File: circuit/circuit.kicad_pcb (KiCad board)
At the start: 4 copper layers, 175.5 x 119.5 mm, 206 parts, among them J201 Barrel_Jack, J301 FX_R_2, J302 FX_R_4, J303 FX_R_6, J304 FX_R_8, J305 FX_R_1, J306 FX_R_3, J307 FX_R_5, J308 FX_R_7, J309 FX_S_1, J310 FX_S_2, J311 FX_S_3, J312 FX_S_4, J313 FX_S_5, J314 FX_S_6, J315 FX_S_7, J316 FX_S_8, J317 Guitar_In, J318 Amp_Out, SW101 Pedal_1, SW102 Pedal_2, SW103 Pedal_3, SW104 Pedal_4, SW105 Pedal_5, SW106 Pedal_6, SW107 Pedal_7, SW108 Pedal_8, SW109 Program, SW110 Preset, U101 ESP32-S3-DevKitC, U201 TMA-1215D, U202 LM7805_TO220, U203 LM7905_TO220, U204 LM1117T-3.3, U301 TL072, U302 TL072, U303 TL072, U304 TL072, U305 TL072, U306 TL072, U307 TL072, U308 TL072, U309 TL072, U401 ADG419BN, U402 CD4051B, U501 CD4051B, U502 CD4051B, U503 CD4051B, U504 CD4051B, U601 CD4051B, U602 CD4051B, U603 CD4051B, U604 CD4051B, U701 74HC595, U702 74HC595, U703 74HC595, U704 74HC595, U801 74HC595, U802 74HC595, U901 74HC595, U902 74HC595

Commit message: Circuit tweaks and PCB
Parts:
- removed L309, L310: 600R@100Mhz, WE-UKW:WE-UKW_74275010
- added C337: 1uF, Capacitor_THT:C_Disc_D3.0mm_W2.0mm_P2.50mm, F.Cu at (122.0, 84.0)
- added L303: 600R@100Mhz, WE-UKW:WE-UKW_74275010, F.Cu at (87.5, 65.5)
- added L304: 600R@100Mhz, WE-UKW:WE-UKW_74275010, F.Cu at (89.0, 79.0)
- C309, C310, C311, C312, C313, C314, C315, C316, C317, C318: value 0.1uF -> 1uF
- C325, C326, C327, C328, C329, C330, C331, C332, C333, C336: value 1uF -> 0.1uF
- D201: value 1N4007 -> 1N5822
- J301: value FX_R_2 -> FX_R_1
- J302: value FX_R_4 -> FX_R_2
- J303: value FX_R_6 -> FX_R_3
- J304: value FX_R_8 -> FX_R_4
- J305: value FX_R_1 -> FX_R_5
- J306: value FX_R_3 -> FX_R_6
- J307: value FX_R_5 -> FX_R_7
- J308: value FX_R_7 -> FX_R_8
- SW102: value Pedal_2 -> Pedal_6
- SW103: value Pedal_3 -> Pedal_2
- SW104: value Pedal_4 -> Pedal_7
- SW105: value Pedal_5 -> Pedal_3
- SW106: value Pedal_6 -> Pedal_8
- SW107: value Pedal_7 -> Pedal_4
- SW108: value Pedal_8 -> Program
- SW109: value Program -> Pedal_5
- moved R902 79.6 mm to (156.7, 133.5)
- moved C318 78.7 mm to (153.5, 46.5), turned to -90 degrees
- moved C314 77.4 mm to (127.4, 46.5), turned to -90 degrees
- moved C110 76.5 mm to (211.5, 39.0)
- moved SW110 76.5 mm to (209.0, 44.0)
- moved C316 75.3 mm to (140.4, 46.5), turned to -90 degrees
- moved R901 73.2 mm to (156.7, 129.0)
- moved R907 72.0 mm to (178.9, 133.5)
- moved C310 70.6 mm to (101.2, 46.5), turned to -90 degrees
- moved R908 69.6 mm to (190.0, 128.9)
- moved C312 68.7 mm to (114.3, 46.5), turned to -90 degrees
- moved R904 68.4 mm to (167.8, 133.4)
- moved C317 66.7 mm to (147.0, 46.5), turned to -90 degrees
- moved C313 66.3 mm to (120.8, 46.5), turned to -90 degrees
- moved R905 65.8 mm to (178.9, 129.0)
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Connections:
- C102 pad 2: Net-(U101-GPIO7/ADC1_CH6) -> Net-(U101-GPIO11/ADC2_CH0)
- C103 pad 2: Net-(U101-GPIO8/ADC1_CH7) -> Net-(U101-GPIO7/ADC1_CH6)
- C104 pad 2: Net-(U101-GPIO9/ADC1_CH8) -> Net-(U101-GPIO12/ADC2_CH1)
- C105 pad 2: Net-(U101-GPIO10/ADC1_CH9) -> Net-(U101-GPIO8/ADC1_CH7)
- C106 pad 2: Net-(U101-GPIO11/ADC2_CH0) -> Net-(U101-GPIO13/ADC2_CH2)
- C107 pad 2: Net-(U101-GPIO12/ADC2_CH1) -> Net-(U101-GPIO9/ADC1_CH8)
- C108 pad 2: Net-(U101-GPIO13/ADC2_CH2) -> Net-(U101-GPIO14/ADC2_CH3)
- C109 pad 2: Net-(U101-GPIO14/ADC2_CH3) -> Net-(U101-GPIO10/ADC1_CH9)
- C309 pad 1: _15V_F -> Net-(C309-Pad1)
- C309 pad 2: AGND -> Net-(C309-Pad2)
- C310 pad 1: _15V_F -> Net-(C310-Pad1)
- C310 pad 2: AGND -> Net-(C310-Pad2)
- C311 pad 1: _15V_F -> Net-(C311-Pad1)
- C311 pad 2: AGND -> Net-(C311-Pad2)
- C312 pad 1: _15V_F -> Net-(C312-Pad1)
- C312 pad 2: AGND -> Net-(C312-Pad2)
- C313 pad 1: AGND -> Net-(C313-Pad1)
- C313 pad 2: +15V_F -> Net-(C313-Pad2)
- C314 pad 1: AGND -> Net-(C314-Pad1)
- C314 pad 2: +15V_F -> Net-(C314-Pad2)
- C315 pad 1: AGND -> Net-(C315-Pad1)
- C315 pad 2: +15V_F -> Net-(C315-Pad2)
- C316 pad 1: AGND -> Net-(C316-Pad1)
- C316 pad 2: +15V_F -> Net-(C316-Pad2)
- C317 pad 1: Net-(U305-V-) -> Net-(C317-Pad1)
- C317 pad 2: AGND -> Net-(C317-Pad2)
- C318 pad 1: Net-(U305-V-) -> Net-(C318-Pad1)
- C318 pad 2: AGND -> Net-(U309-2-)
- C319 pad 1: Net-(U305-V-) -> AGND
- C319 pad 2: AGND -> +15V_F
- C320 pad 1: Net-(U305-V-) -> -15V_F
- C321 pad 2: Net-(U305-V+) -> +15V_F
- C322 pad 1: AGND -> -15V_F
- C322 pad 2: Net-(U305-V+) -> AGND
- C323 pad 2: Net-(U305-V+) -> +15V_F
- C324 pad 1: AGND -> -15V_F
- C324 pad 2: Net-(U305-V+) -> AGND
- C325 pad 1: Net-(C325-Pad1) -> AGND
- C325 pad 2: Net-(C325-Pad2) -> +15V_F
- C326 pad 1: Net-(C326-Pad1) -> -15V_F
- C326 pad 2: Net-(C326-Pad2) -> AGND
- C327 pad 1: Net-(C327-Pad1) -> AGND
- C327 pad 2: Net-(C327-Pad2) -> Net-(U305-V+)
- C328 pad 1: Net-(C328-Pad1) -> Net-(U305-V-)
- C328 pad 2: Net-(C328-Pad2) -> AGND
- C329 pad 1: Net-(C329-Pad1) -> AGND
- C329 pad 2: Net-(C329-Pad2) -> Net-(U305-V+)
- C330 pad 1: Net-(C330-Pad1) -> Net-(U305-V-)
- C330 pad 2: Net-(C330-Pad2) -> AGND
- C331 pad 1: Net-(C331-Pad1) -> AGND
- C331 pad 2: Net-(C331-Pad2) -> Net-(U305-V+)
- C332 pad 1: Net-(C332-Pad1) -> Net-(U305-V-)
- C332 pad 2: Net-(C332-Pad2) -> AGND
- C333 pad 1: Net-(C333-Pad1) -> AGND
- C333 pad 2: Net-(C333-Pad2) -> Net-(U305-V+)
- C336 pad 1: Net-(U309-1-) -> Net-(U305-V-)
- C336 pad 2: GUITAR_IN -> AGND
- C402 pad 1: +5V_F -> -15V_F
- C403 pad 1: -5V_F -> +5V_F
- C404 pad 1: AGND -> -5V_F
- C404 pad 2: +5V_F -> AGND
- C405 pad 1: -15V_F -> AGND
- C405 pad 2: AGND -> +5V_F
- C501 pad 1: AGND -> -5V_F
- C501 pad 2: +5V_F -> AGND
- C503 pad 1: AGND -> -5V_F
- C503 pad 2: +5V_F -> AGND
- C504 pad 1: -5V_F -> AGND
- C504 pad 2: AGND -> +5V_F
- C506 pad 1: -5V_F -> AGND
- C506 pad 2: AGND -> +5V_F
- C507 pad 1: AGND -> -5V_F
- C507 pad 2: +5V_F -> AGND
- C508 pad 1: -5V_F -> AGND
- C508 pad 2: AGND -> +5V_F
- C601 pad 1: AGND -> Net-(U601-VEE)
- C601 pad 2: Net-(U601-VDD) -> AGND
- C602 pad 1: AGND -> Net-(U601-VEE)
- C602 pad 2: Net-(U601-VDD) -> AGND
- C604 pad 1: Net-(U601-VEE) -> AGND
- C604 pad 2: AGND -> Net-(U601-VDD)
- C606 pad 1: Net-(U601-VEE) -> AGND
- C606 pad 2: AGND -> Net-(U601-VDD)
- C607 pad 1: AGND -> Net-(U601-VEE)
- C607 pad 2: Net-(U601-VDD) -> AGND
- C608 pad 1: Net-(U601-VEE) -> AGND
- C608 pad 2: AGND -> Net-(U601-VDD)
- J201 pad 1: GND -> /Power/12V_RAW_1
- J201 pad 2: /Power/12V_RAW_1 -> GND
- J301 pad T: Net-(C303-Pad1) -> Net-(C301-Pad1)
- J302 pad T: Net-(C304-Pad1) -> Net-(C302-Pad1)
- J303 pad T: Net-(C301-Pad1) -> Net-(C303-Pad1)
- J304 pad T: Net-(C302-Pad1) -> Net-(C304-Pad1)
- J309 pad T: Net-(C325-Pad1) -> Net-(C309-Pad1)
- J310 pad T: Net-(C326-Pad1) -> Net-(C310-Pad1)
- J311 pad T: Net-(C327-Pad1) -> Net-(C311-Pad1)
- J312 pad T: Net-(C328-Pad1) -> Net-(C312-Pad1)
- J313 pad T: Net-(C329-Pad1) -> Net-(C313-Pad1)
- J314 pad T: Net-(C330-Pad1) -> Net-(C314-Pad1)
- J315 pad T: Net-(C331-Pad1) -> Net-(C315-Pad1)
- J316 pad T: Net-(C332-Pad1) -> Net-(C316-Pad1)
- J317 pad T: Net-(C333-Pad1) -> Net-(C317-Pad1)
- J318 pad T: Net-(U309-2-) -> Net-(C318-Pad1)
- L301 pad 1: +15V -> +15V_F
- L301 pad 2: +15V_F -> +15V
- L302 pad 1: _15V_F -> -15V
- L302 pad 2: -15V -> -15V_F
- R301 pad 1: Net-(U301-2+) -> Net-(U301-1+)
- R301 pad 2: Net-(C303-Pad2) -> Net-(C301-Pad2)
- R302 pad 1: Net-(U304-2+) -> Net-(U301-2+)
- R303 pad 1: Net-(U302-2+) -> Net-(U302-1+)
- R303 pad 2: Net-(C304-Pad2) -> Net-(C303-Pad2)
- R304 pad 1: Net-(U303-2+) -> Net-(U302-2+)
- R304 pad 2: Net-(C301-Pad2) -> Net-(C304-Pad2)
- R305 pad 1: Net-(U301-1+) -> Net-(U303-1+)
- R306 pad 1: Net-(U302-1+) -> Net-(U303-2+)
- R307 pad 1: Net-(U303-1+) -> Net-(U304-1+)
- R308 pad 1: Net-(U304-1+) -> Net-(U304-2+)
- R309 pad 2: Net-(C325-Pad2) -> Net-(C309-Pad2)
- R310 pad 2: Net-(C326-Pad2) -> Net-(C310-Pad2)
- R311 pad 2: Net-(C327-Pad2) -> Net-(C311-Pad2)
- R312 pad 2: Net-(C328-Pad2) -> Net-(C312-Pad2)
- R313 pad 2: Net-(C329-Pad2) -> Net-(C313-Pad2)
- R314 pad 2: Net-(C330-Pad2) -> Net-(C314-Pad2)
- R315 pad 2: Net-(C331-Pad2) -> Net-(C315-Pad2)
- R316 pad 2: Net-(C332-Pad2) -> Net-(C316-Pad2)
- R317 pad 2: Net-(C333-Pad2) -> Net-(C317-Pad2)
- SW102 pad 1: Net-(U101-GPIO7/ADC1_CH6) -> Net-(U101-GPIO11/ADC2_CH0)
- SW103 pad 1: Net-(U101-GPIO8/ADC1_CH7) -> Net-(U101-GPIO7/ADC1_CH6)
- SW104 pad 1: Net-(U101-GPIO9/ADC1_CH8) -> Net-(U101-GPIO12/ADC2_CH1)
- SW105 pad 1: Net-(U101-GPIO10/ADC1_CH9) -> Net-(U101-GPIO8/ADC1_CH7)
- SW106 pad 1: Net-(U101-GPIO11/ADC2_CH0) -> Net-(U101-GPIO13/ADC2_CH2)
- SW107 pad 1: Net-(U101-GPIO12/ADC2_CH1) -> Net-(U101-GPIO9/ADC1_CH8)
- SW108 pad 1: Net-(U101-GPIO13/ADC2_CH2) -> Net-(U101-GPIO14/ADC2_CH3)
- SW109 pad 1: Net-(U101-GPIO14/ADC2_CH3) -> Net-(U101-GPIO10/ADC1_CH9)
- U301 pad 4: _15V_F -> -15V_F
- U302 pad 4: _15V_F -> -15V_F
- U303 pad 4: _15V_F -> -15V_F
- U304 pad 4: _15V_F -> -15V_F
- U501 pad 10: /Matrix Shift Registers/U8_Q3 -> /IO Routing/U7_Q5
- U501 pad 11: /Matrix Shift Registers/U8_Q2 -> /IO Routing/U7_Q4
- U501 pad 14: FX_R_1 -> FX_R_2
- U501 pad 15: FX_R_2 -> FX_R_3
- U501 pad 3: FX_S_3 -> FX_S_1
- U501 pad 6: /IO Routing/U901_Q3 -> /IO Routing/U901_Q1
- U501 pad 9: /Matrix Shift Registers/U8_Q4 -> /IO Routing/U7_Q6
- U502 pad 10: /IO Routing/U7_Q5 -> /Matrix Shift Registers/U8_Q6
- U502 pad 11: /IO Routing/U7_Q4 -> /Matrix Shift Registers/U8_Q5
- U502 pad 12: FX_R_4 -> FX_R_3
- U502 pad 14: FX_R_2 -> FX_R_1
- U502 pad 15: FX_R_3 -> FX_R_2
- U502 pad 3: FX_S_1 -> FX_S_4
- U502 pad 6: /IO Routing/U901_Q1 -> /IO Routing/U901_Q4
- U502 pad 9: /IO Routing/U7_Q6 -> /Matrix Shift Registers/U8_Q7
- U504 pad 10: /Matrix Shift Registers/U8_Q6 -> /Matrix Shift Registers/U8_Q3
- U504 pad 11: /Matrix Shift Registers/U8_Q5 -> /Matrix Shift Registers/U8_Q2
- U504 pad 12: FX_R_3 -> FX_R_4
- U504 pad 3: FX_S_4 -> FX_S_3
- U504 pad 6: /IO Routing/U901_Q4 -> /IO Routing/U901_Q3
- U504 pad 9: /Matrix Shift Registers/U8_Q7 -> /Matrix Shift Registers/U8_Q4
- U602 pad 10: /Matrix Shift Registers/U9_Q4 -> /Matrix Shift Registers/U10_Q2
- U602 pad 11: /Matrix Shift Registers/U9_Q3 -> /Matrix Shift Registers/U10_Q1
- U602 pad 2: FX_R_7 -> FX_R_6
- U602 pad 3: FX_S_6 -> FX_S_8
- U602 pad 4: FX_R_8 -> FX_R_7
- U602 pad 6: /Inhibit Registers/U902_Q1 -> /Inhibit Registers/U902_Q3
- U602 pad 9: /Matrix Shift Registers/U9_Q5 -> /Matrix Shift Registers/U10_Q3
- U603 pad 10: /Matrix Shift Registers/U9_Q7 -> /Matrix Shift Registers/U9_Q4
- U603 pad 11: /Matrix Shift Registers/U9_Q6 -> /Matrix Shift Registers/U9_Q3
- U603 pad 2: FX_R_6 -> FX_R_7
- U603 pad 3: FX_S_7 -> FX_S_6
- U603 pad 6: /Inhibit Registers/U902_Q2 -> /Inhibit Registers/U902_Q1
- U603 pad 9: /Matrix Shift Registers/U10_Q0 -> /Matrix Shift Registers/U9_Q5
- U604 pad 10: /Matrix Shift Registers/U10_Q2 -> /Matrix Shift Registers/U9_Q7
- U604 pad 11: /Matrix Shift Registers/U10_Q1 -> /Matrix Shift Registers/U9_Q6
- U604 pad 3: FX_S_8 -> FX_S_7
- U604 pad 4: FX_R_7 -> FX_R_8
- U604 pad 6: /Inhibit Registers/U902_Q3 -> /Inhibit Registers/U902_Q2
- U604 pad 9: /Matrix Shift Registers/U10_Q3 -> /Matrix Shift Registers/U10_Q0
- U702 pad 1: /Matrix Shift Registers/U8_Q1 -> /Matrix Shift Registers/U9_Q1
- U702 pad 14: Net-(U701-QH') -> Net-(U702-SER)
- U702 pad 15: /Matrix Shift Registers/U8_Q0 -> /Matrix Shift Registers/U9_Q0
- U702 pad 2: /Matrix Shift Registers/U8_Q2 -> /Matrix Shift Registers/U9_Q2
- U702 pad 3: /Matrix Shift Registers/U8_Q3 -> /Matrix Shift Registers/U9_Q3
- U702 pad 4: /Matrix Shift Registers/U8_Q4 -> /Matrix Shift Registers/U9_Q4
- U702 pad 5: /Matrix Shift Registers/U8_Q5 -> /Matrix Shift Registers/U9_Q5
- U702 pad 6: /Matrix Shift Registers/U8_Q6 -> /Matrix Shift Registers/U9_Q6
- U702 pad 7: /Matrix Shift Registers/U8_Q7 -> /Matrix Shift Registers/U9_Q7
- U703 pad 1: /Matrix Shift Registers/U9_Q1 -> /Matrix Shift Registers/U8_Q1
- U703 pad 14: Net-(U702-QH') -> Net-(U701-QH')
- U703 pad 15: /Matrix Shift Registers/U9_Q0 -> /Matrix Shift Registers/U8_Q0
- U703 pad 2: /Matrix Shift Registers/U9_Q2 -> /Matrix Shift Registers/U8_Q2
- U703 pad 3: /Matrix Shift Registers/U9_Q3 -> /Matrix Shift Registers/U8_Q3
- U703 pad 4: /Matrix Shift Registers/U9_Q4 -> /Matrix Shift Registers/U8_Q4
- U703 pad 5: /Matrix Shift Registers/U9_Q5 -> /Matrix Shift Registers/U8_Q5
- U703 pad 6: /Matrix Shift Registers/U9_Q6 -> /Matrix Shift Registers/U8_Q6
- U703 pad 7: /Matrix Shift Registers/U9_Q7 -> /Matrix Shift Registers/U8_Q7
- U703 pad 9: Net-(U703-QH') -> Net-(U702-SER)
- U704 pad 14: Net-(U703-QH') -> Net-(U702-QH')
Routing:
- net /Matrix Shift Registers/U8_Q0: track 22.9 -> 162.7 mm
- net /Inhibit Registers/U902_Q0: track 70.7 -> 202.7 mm
- net FX_S_1: track 147.4 -> 31.7 mm
- net /Matrix Shift Registers/U8_Q3: track 40.5 -> 150.4 mm
- net /IO Routing/U7_Q4: track 75.8 -> 185.8 mm
- net /IO Routing/U901_Q1: track 187.3 -> 82.1 mm
- net Net-(Disp101-SDA): track 69.6 -> 168.5 mm
- net /Matrix Shift Registers/U8_Q4: track 43.1 -> 139.8 mm
- net Net-(U101-GPIO14/ADC2_CH3): track 77.2 -> 169.9 mm
- net -15V_F: track 9.39 -> 78.6 mm
- net /Matrix Shift Registers/U8_Q2: track 43.1 -> 109.3 mm
- net /Matrix Shift Registers/U8_Q1: track 22.4 -> 87.6 mm
- net _15V_F: track 62.3 -> 0.00 mm
- net Net-(U101-GPIO15/ADC2_CH4/32K_P): track 147.5 -> 86.1 mm
- net Net-(U601-VDD): track 66.2 -> 127.1 mm
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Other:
- board size 175.5 x 119.5 mm -> 175.5 x 120.8 mm

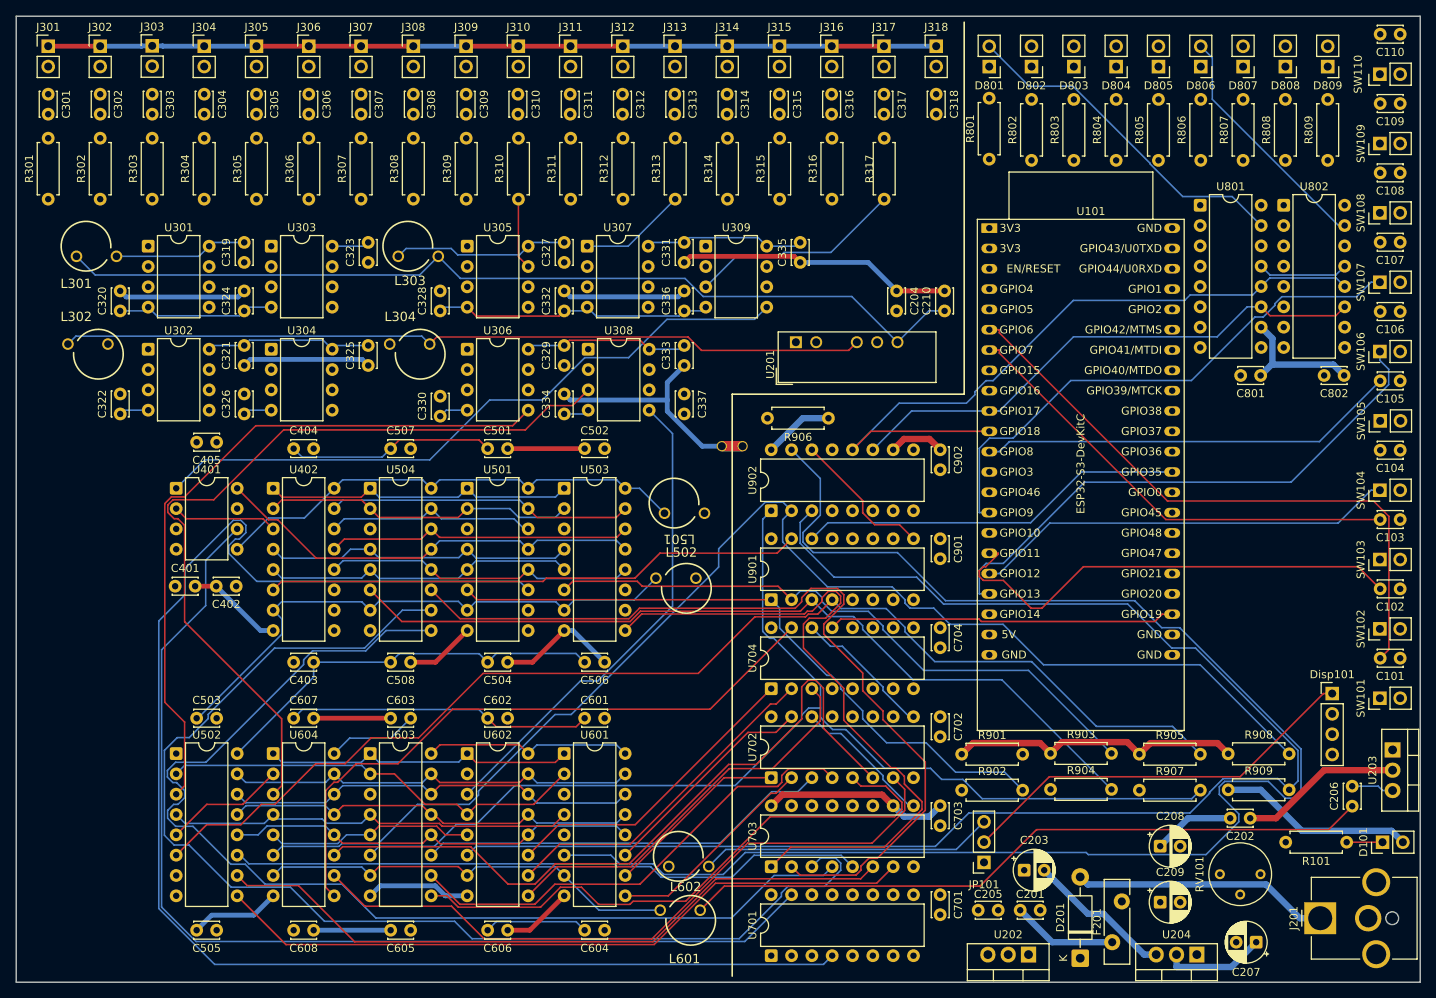
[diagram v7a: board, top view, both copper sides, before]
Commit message: Labels for headers on PCB
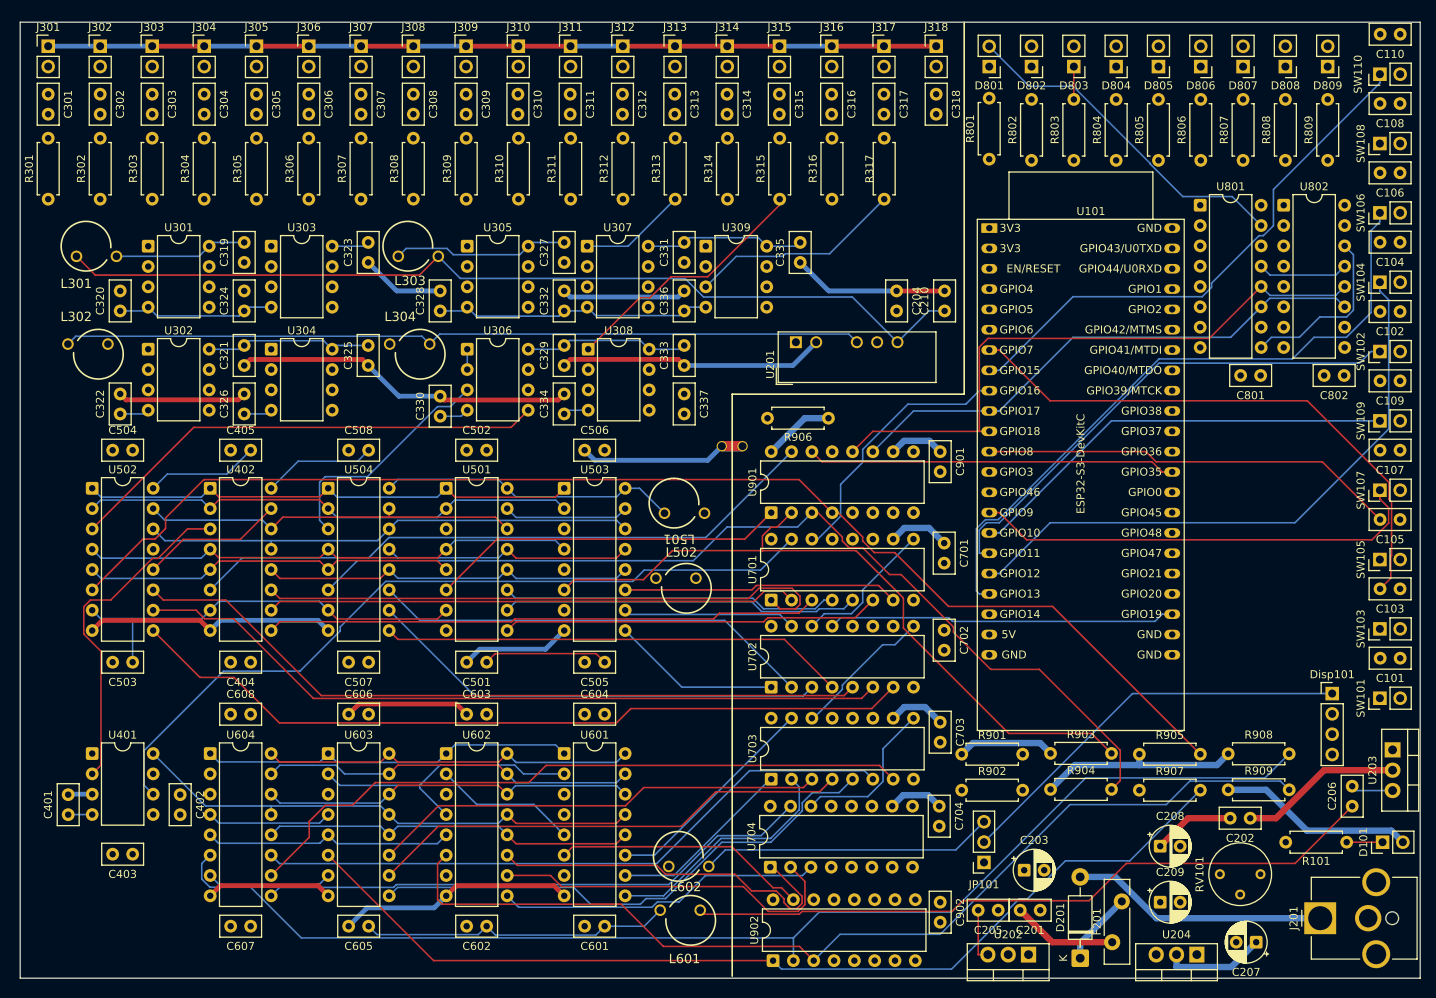
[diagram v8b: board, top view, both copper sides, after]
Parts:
- C101, C102, C103, C104, C105, C106, C107, C108, C109, C110, C201, C202, C204, C205, C206, C210, C301, C302, C303, C304, C305, C306, C307, C308, C309, C310, C311, C312, C313, C314, C315, C316, C317, C318, C319, C320, C321, C322, C323, C324, C325, C326, C327, C328, C329, C330, C331, C332, C333, C334, C335, C336, C337, C401, C402, C403, C404, C405, C501, C502, C503, C504, C505, C506, C507, C508, C601, C602, C603, C604, C605, C606, C607, C608, C701, C702, C703, C704, C801, C802, C901, C902: footprint Capacitor_THT:C_Disc_D3.0mm_W2.0mm_P2.50mm -> Capacitor_THT:C_Disc_D5.0mm_W2.5mm_P2.50mm
- moved C505 58.9 mm to (112.1, 117.5)
- moved C902 56.6 mm to (154.0, 147.5)
- moved U902 56.2 mm to (133.1, 154.8)
- moved C504 56.0 mm to (50.6, 91.0), turned to 0 degrees
- moved U701 44.4 mm to (132.9, 109.7)
- moved C701 44.0 mm to (154.5, 102.6)
- moved U401 34.8 mm to (48.0, 128.9)
- moved U502 34.8 mm to (48.0, 95.8)
- moved C109 34.7 mm to (211.5, 82.3)
- moved C102 34.7 mm to (211.5, 73.7)
- moved SW109 34.7 mm to (209.0, 87.3)
- moved SW102 34.7 mm to (209.0, 78.7)
- moved C606 33.5 mm to (80.1, 124.0), turned to 0 degrees
- moved C403 33.0 mm to (53.1, 141.5)
- moved C401 31.5 mm to (45.0, 136.6), turned to 90 degrees
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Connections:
- net /IO Routing/U7_Q0 renamed /IO Routing/U701_Q0
- net /IO Routing/U7_Q1 renamed /IO Routing/U701_Q1
- net /IO Routing/U7_Q2 renamed /IO Routing/U701_Q2
- net /IO Routing/U7_Q3 renamed /IO Routing/U701_Q3
- net /IO Routing/U7_Q4 renamed /IO Routing/U701_Q4
- net /IO Routing/U7_Q5 renamed /IO Routing/U701_Q5
- net /IO Routing/U7_Q6 renamed /IO Routing/U701_Q6
- net /IO Routing/U7_Q7 renamed /IO Routing/U701_Q7
- net /Matrix Shift Registers/U10_Q0 renamed /Matrix Shift Registers/U704_Q0
- net /Matrix Shift Registers/U10_Q1 renamed /Matrix Shift Registers/U704_Q1
- net /Matrix Shift Registers/U10_Q2 renamed /Matrix Shift Registers/U704_Q2
- net /Matrix Shift Registers/U10_Q3 renamed /Matrix Shift Registers/U704_Q3
- U502 pad 10: /Matrix Shift Registers/U8_Q6 -> /Matrix Shift Registers/U702_Q6
- U502 pad 11: /Matrix Shift Registers/U8_Q5 -> /Matrix Shift Registers/U702_Q5
- U502 pad 9: /Matrix Shift Registers/U8_Q7 -> /Matrix Shift Registers/U702_Q7
- U503 pad 10: /Matrix Shift Registers/U8_Q0 -> /Matrix Shift Registers/U702_Q0
- U503 pad 9: /Matrix Shift Registers/U8_Q1 -> /Matrix Shift Registers/U702_Q1
- U504 pad 10: /Matrix Shift Registers/U8_Q3 -> /Matrix Shift Registers/U702_Q3
- U504 pad 11: /Matrix Shift Registers/U8_Q2 -> /Matrix Shift Registers/U702_Q2
- U504 pad 9: /Matrix Shift Registers/U8_Q4 -> /Matrix Shift Registers/U702_Q4
- U601 pad 10: /Matrix Shift Registers/U9_Q1 -> /Matrix Shift Registers/U703_Q1
- U601 pad 11: /Matrix Shift Registers/U9_Q0 -> /Matrix Shift Registers/U703_Q0
- U601 pad 9: /Matrix Shift Registers/U9_Q2 -> /Matrix Shift Registers/U703_Q2
- U603 pad 10: /Matrix Shift Registers/U9_Q4 -> /Matrix Shift Registers/U703_Q4
- U603 pad 11: /Matrix Shift Registers/U9_Q3 -> /Matrix Shift Registers/U703_Q3
- U603 pad 9: /Matrix Shift Registers/U9_Q5 -> /Matrix Shift Registers/U703_Q5
- U604 pad 10: /Matrix Shift Registers/U9_Q7 -> /Matrix Shift Registers/U703_Q7
- U604 pad 11: /Matrix Shift Registers/U9_Q6 -> /Matrix Shift Registers/U703_Q6
- U702 pad 1: /Matrix Shift Registers/U9_Q1 -> /Matrix Shift Registers/U702_Q1
- U702 pad 14: Net-(U702-SER) -> Net-(U701-QH')
- U702 pad 15: /Matrix Shift Registers/U9_Q0 -> /Matrix Shift Registers/U702_Q0
- U702 pad 2: /Matrix Shift Registers/U9_Q2 -> /Matrix Shift Registers/U702_Q2
- U702 pad 3: /Matrix Shift Registers/U9_Q3 -> /Matrix Shift Registers/U702_Q3
- U702 pad 4: /Matrix Shift Registers/U9_Q4 -> /Matrix Shift Registers/U702_Q4
- U702 pad 5: /Matrix Shift Registers/U9_Q5 -> /Matrix Shift Registers/U702_Q5
- U702 pad 6: /Matrix Shift Registers/U9_Q6 -> /Matrix Shift Registers/U702_Q6
- U702 pad 7: /Matrix Shift Registers/U9_Q7 -> /Matrix Shift Registers/U702_Q7
- U703 pad 1: /Matrix Shift Registers/U8_Q1 -> /Matrix Shift Registers/U703_Q1
- U703 pad 14: Net-(U701-QH') -> Net-(U702-QH')
- U703 pad 15: /Matrix Shift Registers/U8_Q0 -> /Matrix Shift Registers/U703_Q0
- U703 pad 2: /Matrix Shift Registers/U8_Q2 -> /Matrix Shift Registers/U703_Q2
- U703 pad 3: /Matrix Shift Registers/U8_Q3 -> /Matrix Shift Registers/U703_Q3
- U703 pad 4: /Matrix Shift Registers/U8_Q4 -> /Matrix Shift Registers/U703_Q4
- U703 pad 5: /Matrix Shift Registers/U8_Q5 -> /Matrix Shift Registers/U703_Q5
- U703 pad 6: /Matrix Shift Registers/U8_Q6 -> /Matrix Shift Registers/U703_Q6
- U703 pad 7: /Matrix Shift Registers/U8_Q7 -> /Matrix Shift Registers/U703_Q7
- U703 pad 9: Net-(U702-SER) -> Net-(U703-QH')
- U704 pad 14: Net-(U702-QH') -> Net-(U703-QH')
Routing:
- net /Matrix Shift Registers/U8_Q0: track 162.7 -> 0.00 mm
- net /Matrix Shift Registers/U8_Q3: track 150.4 -> 0.00 mm
- net /IO Routing/U701_Q4: track 185.8 -> 42.1 mm
- net /Matrix Shift Registers/U8_Q4: track 139.8 -> 0.00 mm
- net /Matrix Shift Registers/U8_Q2: track 109.3 -> 0.00 mm
- net /Inhibit Registers/U902_Q0: track 202.7 -> 94.1 mm
- net /Matrix Shift Registers/U702_Q7: track 0.00 -> 99.1 mm
- net /Matrix Shift Registers/U702_Q6: track 0.00 -> 95.1 mm
- net /Matrix Shift Registers/U702_Q5: track 0.00 -> 93.3 mm
- net /Matrix Shift Registers/U9_Q6: track 90.6 -> 0.00 mm
- net /Matrix Shift Registers/U8_Q7: track 88.6 -> 0.00 mm
- net /Matrix Shift Registers/U8_Q1: track 87.6 -> 0.00 mm
- net /Matrix Shift Registers/U8_Q6: track 86.8 -> 0.00 mm
- net /Matrix Shift Registers/U9_Q7: track 86.0 -> 0.00 mm
- net /Matrix Shift Registers/U703_Q7: track 0.00 -> 85.3 mm
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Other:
- board size 175.5 x 120.8 mm -> 175 x 119.5 mm
- board text added: "Buttons"
- board text added: "Jacks"
- board text added: "LEDs"
